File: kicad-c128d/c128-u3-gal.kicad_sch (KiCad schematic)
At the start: 5 parts, among them J1 Conn_02x04_Row_Letter_Last, J2 Conn_01x02, J3 Conn_01x04, U1 74LS138, U2 GAL20V10

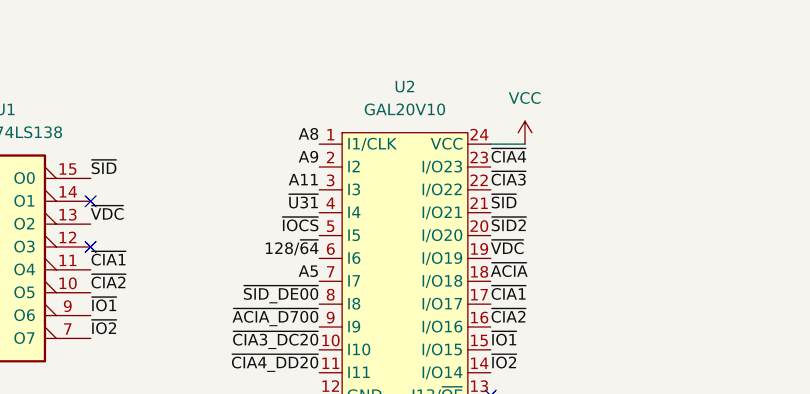
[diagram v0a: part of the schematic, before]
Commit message: correct GAL device name to GAL22V10
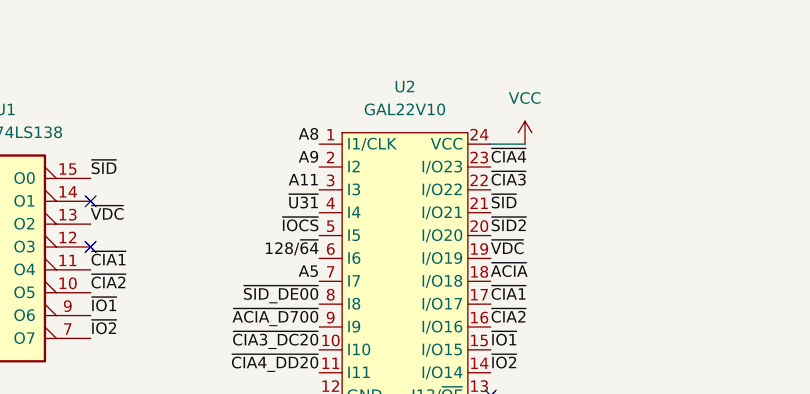
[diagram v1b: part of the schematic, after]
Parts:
- U2: value GAL20V10 -> GAL22V10
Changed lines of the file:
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@@
     (in_bom yes) (on_board yes) (fields_autoplaced)
     (property "Reference" "U2" (id 0) (at 135.255 67.31 0))
-    (property "Value" "GAL20V10" (id 1) (at 135.255 69.85 0))
+    (property "Value" "GAL22V10" (id 1) (at 135.255 69.85 0))
     (property "Footprint" "Package_DIP:DIP-24_W7.62mm_LongPads" (id 2) (at 134.62 69.85 0)
       (effects (font (size 1.27 1.27)) hide)
@@
     )
     (path "/c4b873b6-3fb3-47ef-b812-abfb000cba2a"
-      (reference "U2") (unit 1) (value "GAL20V10") (footprint "Package_DIP:DIP-24_W7.62mm_LongPads")
+      (reference "U2") (unit 1) (value "GAL22V10") (footprint "Package_DIP:DIP-24_W7.62mm_LongPads")
     )
   )
